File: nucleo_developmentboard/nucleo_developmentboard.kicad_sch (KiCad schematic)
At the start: 30 parts, among them J1 Conn_01x03_Socket, J1 Conn_PinHeader_1x05_P2.54mm_V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, J2 Conn_01x03_Socket, J3 Conn_01x02_Socket, J5 MOTOR2 OUT, J7 Conn_01x01_Socket, J8 Conn_01x01_Socket, U1 NUCLEO-L432KC, U2 L293D, U3 LM7805_TO220, U4 HM-11_Module

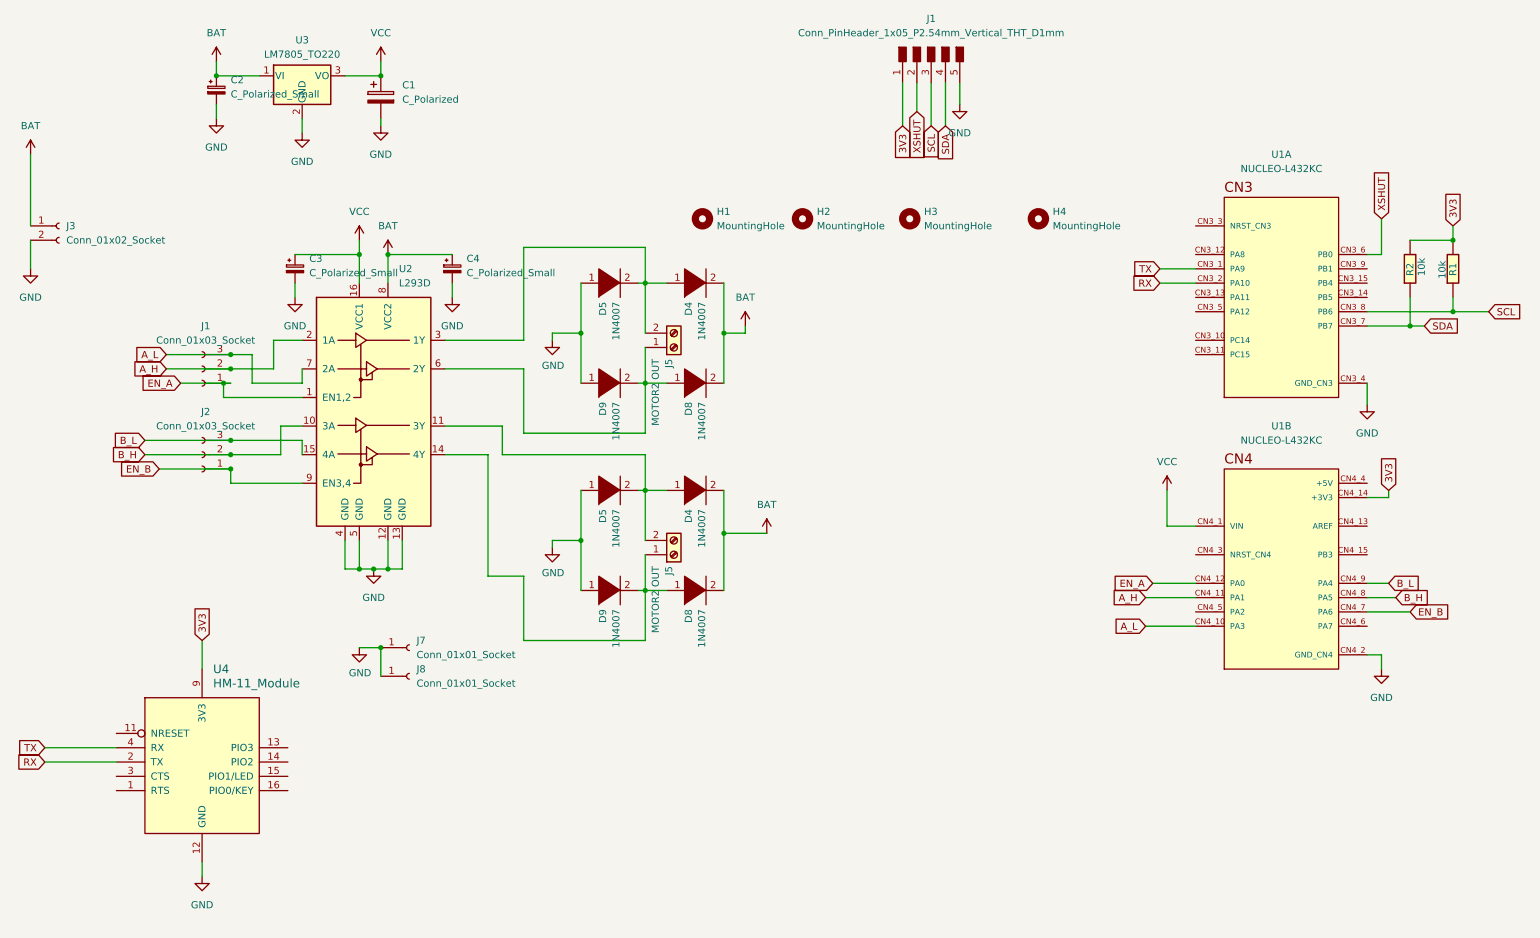
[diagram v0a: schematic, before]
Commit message: updated Nucleo connections and switched to HM11 smd
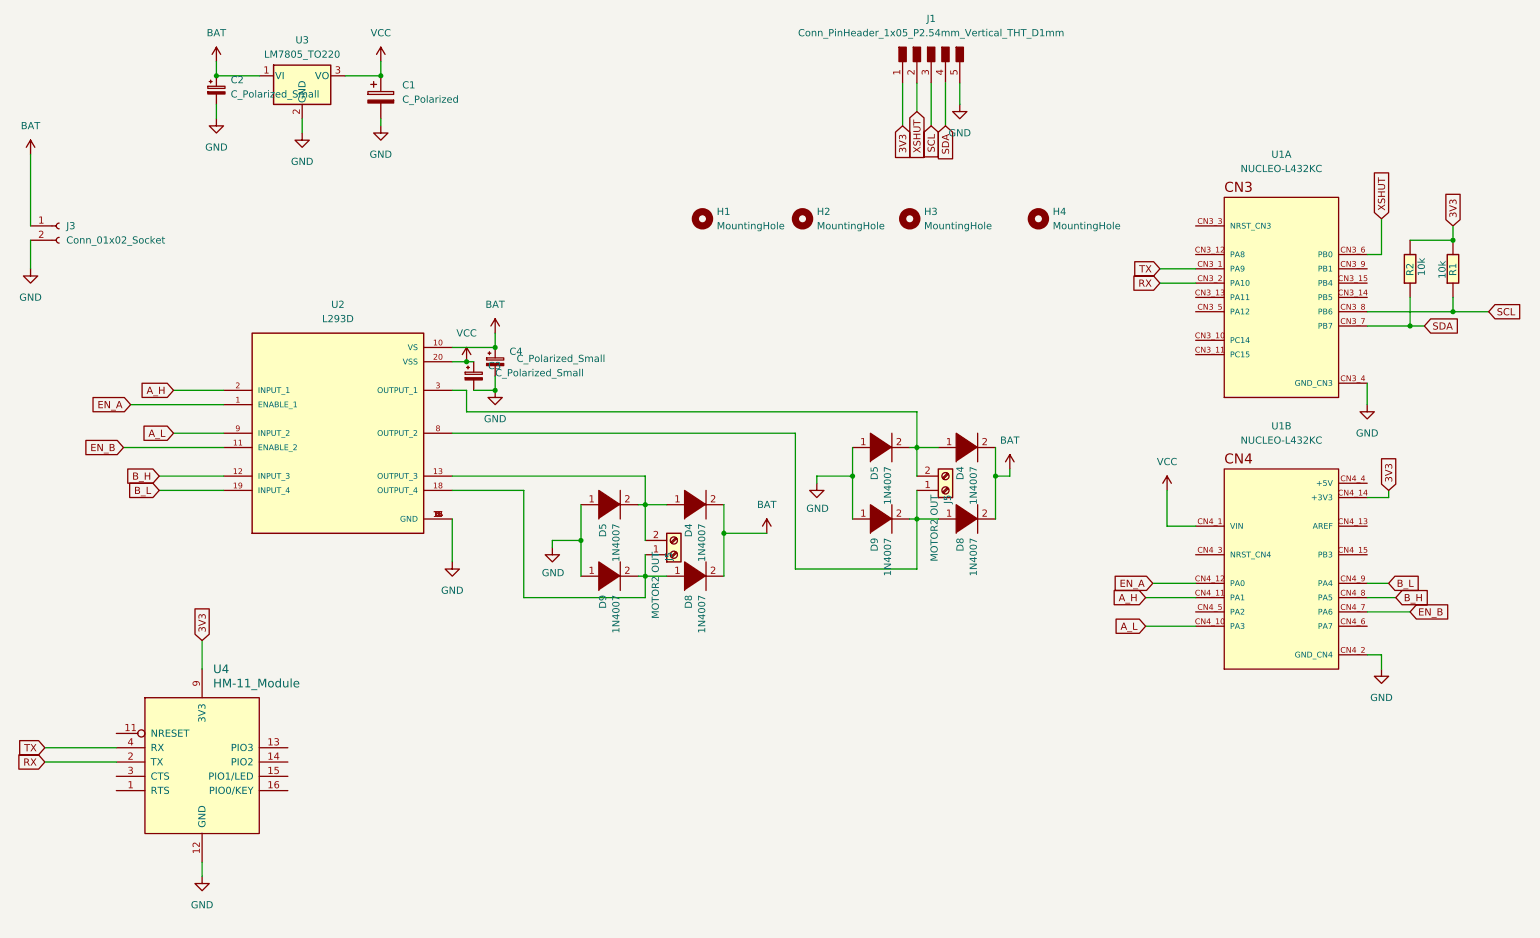
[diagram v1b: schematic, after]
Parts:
- removed J1, J2: Conn_01x03_Socket, Connector_PinHeader_2.54mm:PinHeader_1x03_P2.54mm_Vertical, symbol Connector:Conn_01x03_Socket
- removed J7, J8: Conn_01x01_Socket, Connector_PinHeader_2.54mm:PinHeader_1x01_P2.54mm_Vertical, symbol Connector:Conn_01x01_Socket
- U2: footprint Package_DIP:DIP-16_W7.62mm -> SOIC127P1032X265-20N; symbol Driver_Motor:L293D -> L293DD:L293DD; MANUFACTURER (none) -> STMicroelectronics; PARTREV (none) -> N/A; STANDARD (none) -> IPC-7351B
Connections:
- net +BAT: now also U2.10 (VS); no longer U2.8 (VCC2)
- net A_L: now also U2.9 (INPUT_2); no longer U2.7 (2A)
- net B_H: now also U2.12 (INPUT_3); no longer U2.10 (3A)
- net B_L: now also U2.19 (INPUT_4); no longer U2.15 (4A)
- net EN_B: now also U2.11 (ENABLE_2); no longer U2.9 (EN3,4)
- net GND: now also U2.14 (GND), U2.15 (GND), U2.16 (GND), U2.17 (GND), U2.6 (GND), U2.7 (GND); no longer U2.12 (GND), U2.13 (GND)
- net VCC: now also U2.20 (VSS); no longer U2.16 (VCC1)
- net at D8.1 (K), D9.2 (A), J5.1 (Pin_1): now also U2.8 (OUTPUT_2); no longer U2.6 (2Y)
- net at D4.1 (K), D5.2 (A), J5.2 (Pin_2): now also U2.13 (OUTPUT_3); no longer U2.11 (3Y)
- net at D8.1 (K), D9.2 (A), J5.1 (Pin_1): now also U2.18 (OUTPUT_4); no longer U2.14 (4Y)
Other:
- moved on the sheet: C3, C4, D4, D5, D8, D9, J5

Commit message: Final Nucleo board updated with all SMD components
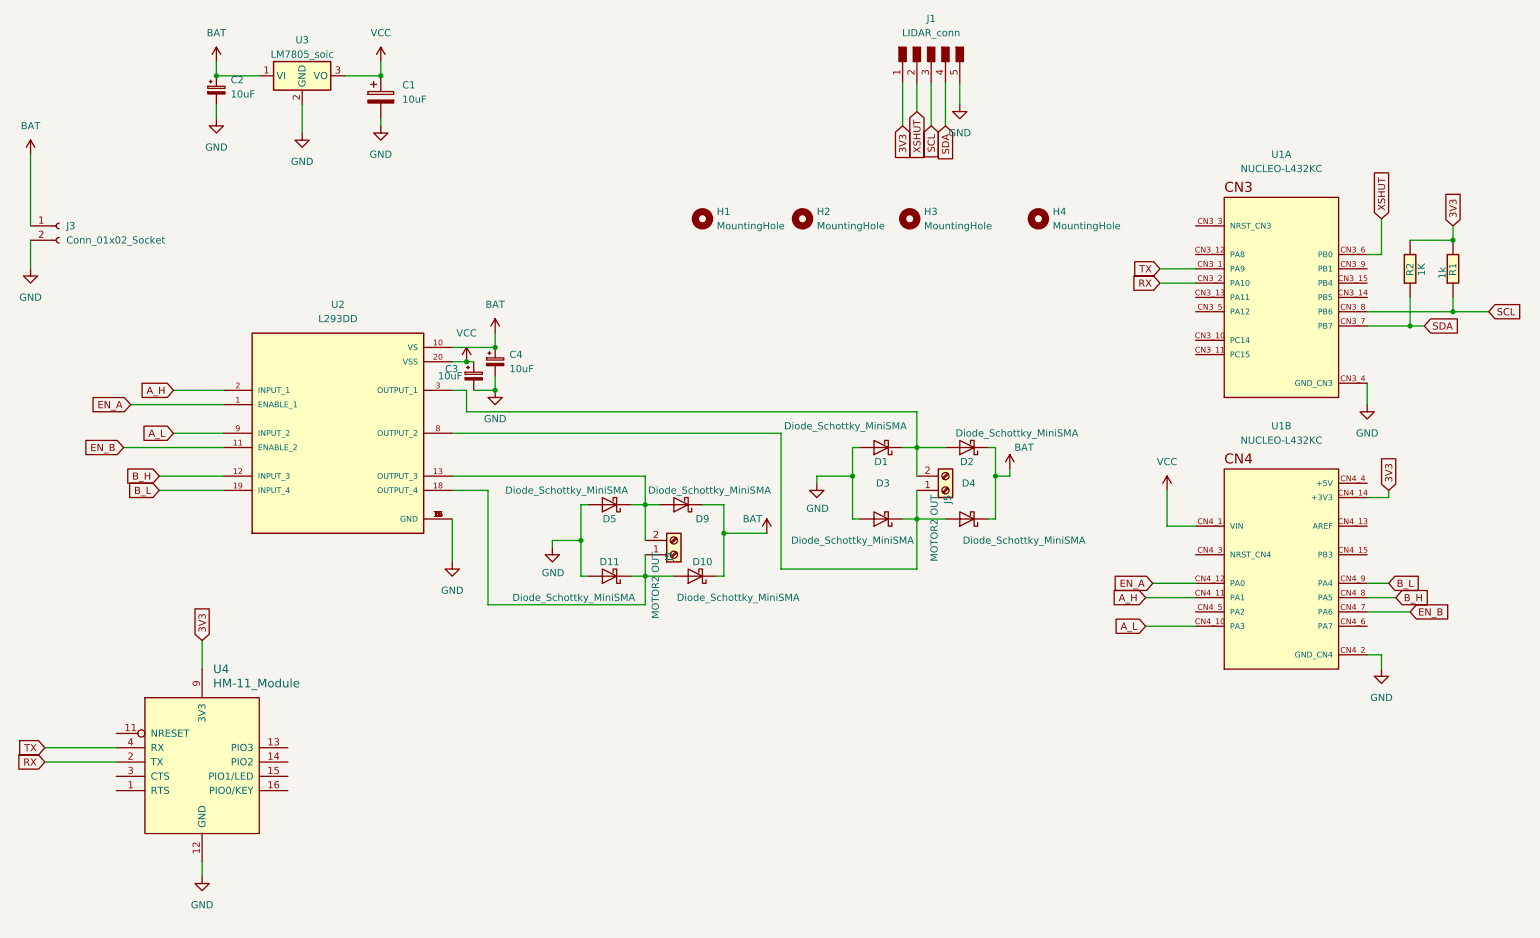
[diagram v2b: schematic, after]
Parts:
- removed D4 (x2), D5 (x2), D8 (x2), D9 (x2): 1N4007, Diode_THT:D_A-405_P7.62mm_Horizontal, symbol L293D Module-rescue:DIODE-pspice
- added D1, D10, D11, D2, D3, D4, D5, D9: Diode_Schottky_MiniSMA, fab:SOD-123T, symbol fab:Diode_Schottky_MiniSMA
- C1: value C_Polarized -> 10uF; footprint Capacitor_THT:CP_Radial_D5.0mm_P2.50mm -> fab:C_1206
- C2, C3, C4: value C_Polarized_Small -> 10uF; footprint Capacitor_THT:CP_Radial_D5.0mm_P2.00mm -> fab:C_1206
- J1: value Conn_PinHeader_1x05_P2.54mm_Vertical_THT_D1mm -> LIDAR_conn
- R1: value 10k -> 1k; footprint Resistor_THT:R_Axial_DIN0204_L3.6mm_D1.6mm_P5.08mm_Horizontal -> fab:R_1206
- R2: value 10k -> 1K; footprint Resistor_THT:R_Axial_DIN0204_L3.6mm_D1.6mm_P5.08mm_Horizontal -> fab:R_1206
- U2: value L293D -> L293DD
- U3: value LM7805_TO220 -> LM7805_soic; footprint Package_TO_SOT_THT:TO-220-3_Vertical -> fab:SOT-223-3_TabPin2; symbol Regulator_Linear:LM7805_TO220 -> fab:Regulator_Linear_5.0V_1A_TexasInstruments
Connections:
- net +BAT: now also D10.1 (K), D2.1 (K), D4.1 (K), D9.1 (K)
- net GND: now also D1.2 (A), D11.2 (A), D3.2 (A), D5.2 (A)
- net at J5.1 (Pin_1), U2.8 (OUTPUT_2): now also D3.1 (K), D4.2 (A)
- net at J5.2 (Pin_2), U2.13 (OUTPUT_3): now also D5.1 (K), D9.2 (A)
- net at J5.2 (Pin_2), U2.3 (OUTPUT_1): now also D1.1 (K), D2.2 (A)
- net at J5.1 (Pin_1), U2.18 (OUTPUT_4): now also D10.2 (A), D11.1 (K)
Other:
- moved on the sheet: U3

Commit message: added LSM303CTR
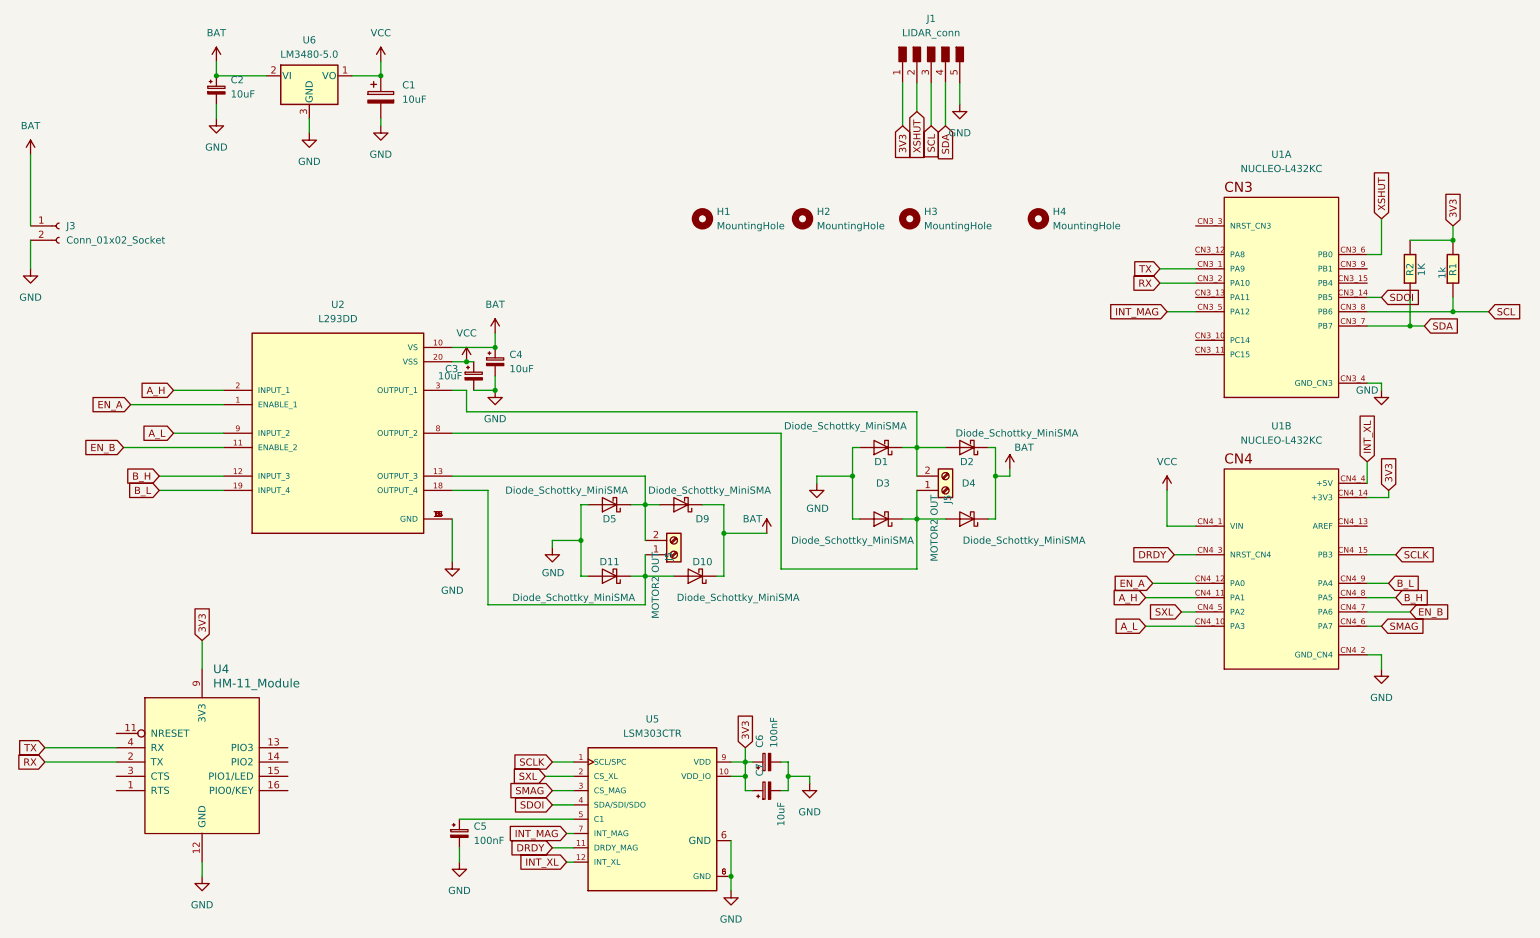
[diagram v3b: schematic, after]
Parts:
- removed U3: LM7805_soic, fab:SOT-223-3_TabPin2, symbol fab:Regulator_Linear_5.0V_1A_TexasInstruments
- added C5, C6: 100nF, fab:C_1206, symbol Device:C_Polarized_Small
- added C7: 10uF, fab:C_1206, symbol Device:C_Polarized_Small
- added U5: LSM303CTR, LSM303CTR:LGA12R50P_200X200X100, symbol LSM303CTR:LSM303CTR
- added U6: LM3480-5.0, Package_TO_SOT_SMD:SOT-23, symbol Regulator_Linear:LM3480-5.0
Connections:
- net +BAT: now also U6.2 (VI)
- net 3V3: now also C6.1, C7.1, U5.10 (VDD_IO), U5.9 (VDD)
- net GND: now also C5.2, C6.2, C7.2, U5.6 (GND), U5.8 (GND), U6.3 (GND)
- net VCC: now also U6.1 (VO)
- net SCLK: now reaches U1.CN4_15 (PB3)
- net SCLK: now also U5.1 (SCL/SPC)
- net DRDY: now reaches U1.CN4_3 (NRST_CN4)
- net DRDY: now also U5.11 (DRDY_MAG)
- net INT_XL: now reaches U1.CN4_4 (+5V)
- net INT_XL: now also U5.12 (INT_XL)
- net SXL: now reaches U1.CN4_5 (PA2)
- net SXL: now also U5.2 (CS_XL)
- net SMAG: now reaches U1.CN4_6 (PA7)
- net SMAG: now also U5.3 (CS_MAG)
- net SDOI: now reaches U1.CN3_14 (PB5)
- net SDOI: now also U5.4 (SDA/SDI/SDO)
- net INT_MAG: now reaches U1.CN3_5 (PA12)
- net INT_MAG: now also U5.7 (INT_MAG)
- new net: C5.1, U5.5 (C1)
